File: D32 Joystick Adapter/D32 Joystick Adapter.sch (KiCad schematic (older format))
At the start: 12 parts, among them J1 Dragon 32, J2 Joystick, U1 4066

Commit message: Layout done
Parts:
- added M1, M2, M3, M4: Mounting, mounting:M3_pin, symbol mounting:Mounting
- C1: footprint Capacitors_THT:C_Disc_D4.7mm_W2.5mm_P5.00mm -> Capacitor_THT:C_Disc_D4.7mm_W2.5mm_P5.00mm
- J1: footprint (none) -> D32_Wirepads:OUTPUT_ZIP
- R1, R2, R3, R4, R5, R6, R7, R8: footprint (none) -> Resistor_THT:R_Axial_DIN0207_L6.3mm_D2.5mm_P10.16mm_Horizontal
- U1: footprint (none) -> Package_DIP:DIP-14_W7.62mm_Socket_LongPads
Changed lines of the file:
@@
 encoding utf-8
 Sheet 1 1
-Title ""
+Title "Dragon 32 Digital Joystick Adapter"
 Date ""
-Rev ""
+Rev "A"
 Comp ""
 Comment1 ""
 Comment2 ""
 Comment3 ""
-Comment4 ""
+Comment4 "Allows the use of Atari-style joysticks on the Dragon 32 computer."
 $EndDescr
 $Comp
@@
 F 0 "C1" H 685 6921 50  0000 R CNN
 F 1 "100nF" H 685 6830 50  0000 R CNN
-F 2 "Capacitors_THT:C_Disc_D4.7mm_W2.5mm_P5.00mm" H 838 6725 50  0001 C CNN
+F 2 "Capacitor_THT:C_Disc_D4.7mm_W2.5mm_P5.00mm" H 838 6725 50  0001 C CNN
 F 3 "~" H 800 6875 50  0001 C CNN
 	1    800  6875
@@
 F 0 "U1" H 4925 4527 50  0000 C CNN
 F 1 "4066" H 4925 4436 50  0000 C CNN
-F 2 "" H 4925 4700 50  0001 C CNN
+F 2 "Package_DIP:DIP-14_W7.62mm_Socket_LongPads" H 4925 4700 50  0001 C CNN
 F 3 "http://www.ti.com/lit/ds/symlink/cd4066b.pdf" H 4925 4700 50  0001 C CNN
 	1    4925 4700
@@
 F 0 "U1" H 4925 5277 50  0000 C CNN
 F 1 "4066" H 4925 5186 50  0000 C CNN
-F 2 "" H 4925 5450 50  0001 C CNN
+F 2 "Package_DIP:DIP-14_W7.62mm_Socket_LongPads" H 4925 5450 50  0001 C CNN
 F 3 "http://www.ti.com/lit/ds/symlink/cd4066b.pdf" H 4925 5450 50  0001 C CNN
 	2    4925 5450
@@
 F 0 "U1" H 7150 5277 50  0000 C CNN
 F 1 "4066" H 7150 5186 50  0000 C CNN
-F 2 "" H 7150 5450 50  0001 C CNN
+F 2 "Package_DIP:DIP-14_W7.62mm_Socket_LongPads" H 7150 5450 50  0001 C CNN
 F 3 "http://www.ti.com/lit/ds/symlink/cd4066b.pdf" H 7150 5450 50  0001 C CNN
 	3    7150 5450
@@
 F 0 "U1" H 7150 4527 50  0000 C CNN
 F 1 "4066" H 7150 4436 50  0000 C CNN
-F 2 "" H 7150 4700 50  0001 C CNN
+F 2 "Package_DIP:DIP-14_W7.62mm_Socket_LongPads" H 7150 4700 50  0001 C CNN
 F 3 "http://www.ti.com/lit/ds/symlink/cd4066b.pdf" H 7150 4700 50  0001 C CNN
 	4    7150 4700
@@
 F 0 "U1" H 1630 6921 50  0000 L CNN
 F 1 "4066" H 1630 6830 50  0000 L CNN
-F 2 "" H 1400 6875 50  0001 C CNN
+F 2 "Package_DIP:DIP-14_W7.62mm_Socket_LongPads" H 1400 6875 50  0001 C CNN
 F 3 "http://www.ti.com/lit/ds/symlink/cd4066b.pdf" H 1400 6875 50  0001 C CNN
 	5    1400 6875
@@
 F 0 "J1" H 6675 1350 50  0000 C CNN
 F 1 "Dragon 32" H 6675 1425 50  0000 C CNN
-F 2 "" H 6675 1925 50  0001 C CNN
+F 2 "D32_Wirepads:OUTPUT_ZIP" H 6675 1925 50  0001 C CNN
 F 3 "http://www.mouser.com/ds/2/18/40_c091_abd_e-75918.pdf" H 6675 1925 50  0001 C CNN
 	1    6675 1925
@@
 F 0 "R2" H 4492 4104 50  0000 R CNN
 F 1 "100k" H 4492 4195 50  0000 R CNN
-F 2 "" H 4550 4150 50  0001 C CNN
+F 2 "Resistor_THT:R_Axial_DIN0207_L6.3mm_D2.5mm_P10.16mm_Horizontal" H 4550 4150 50  0001 C CNN
 F 3 "~" H 4550 4150 50  0001 C CNN
 	1    4550 4150
@@
 F 0 "R1" H 4117 4104 50  0000 R CNN
 F 1 "100k" H 4117 4195 50  0000 R CNN
-F 2 "" H 4175 4150 50  0001 C CNN
+F 2 "Resistor_THT:R_Axial_DIN0207_L6.3mm_D2.5mm_P10.16mm_Horizontal" H 4175 4150 50  0001 C CNN
 F 3 "~" H 4175 4150 50  0001 C CNN
 	1    4175 4150
@@
 F 0 "R3" H 4867 4104 50  0000 R CNN
 F 1 "100k" H 4867 4195 50  0000 R CNN
-F 2 "" H 4925 4150 50  0001 C CNN
+F 2 "Resistor_THT:R_Axial_DIN0207_L6.3mm_D2.5mm_P10.16mm_Horizontal" H 4925 4150 50  0001 C CNN
 F 3 "~" H 4925 4150 50  0001 C CNN
 	1    4925 4150
@@
 F 0 "R4" H 4492 5579 50  0000 R CNN
 F 1 "100k" H 4492 5670 50  0000 R CNN
-F 2 "" H 4550 5625 50  0001 C CNN
+F 2 "Resistor_THT:R_Axial_DIN0207_L6.3mm_D2.5mm_P10.16mm_Horizontal" H 4550 5625 50  0001 C CNN
 F 3 "~" H 4550 5625 50  0001 C CNN
 	1    4550 5625
@@
 F 0 "R6" H 6717 4104 50  0000 R CNN
 F 1 "100k" H 6717 4195 50  0000 R CNN
-F 2 "" H 6775 4150 50  0001 C CNN
+F 2 "Resistor_THT:R_Axial_DIN0207_L6.3mm_D2.5mm_P10.16mm_Horizontal" H 6775 4150 50  0001 C CNN
 F 3 "~" H 6775 4150 50  0001 C CNN
 	1    6775 4150
@@
 F 0 "R5" H 6342 4104 50  0000 R CNN
 F 1 "100k" H 6342 4195 50  0000 R CNN
-F 2 "" H 6400 4150 50  0001 C CNN
+F 2 "Resistor_THT:R_Axial_DIN0207_L6.3mm_D2.5mm_P10.16mm_Horizontal" H 6400 4150 50  0001 C CNN
 F 3 "~" H 6400 4150 50  0001 C CNN
 	1    6400 4150
@@
 F 0 "R7" H 7092 4104 50  0000 R CNN
 F 1 "100k" H 7092 4195 50  0000 R CNN
-F 2 "" H 7150 4150 50  0001 C CNN
+F 2 "Resistor_THT:R_Axial_DIN0207_L6.3mm_D2.5mm_P10.16mm_Horizontal" H 7150 4150 50  0001 C CNN
 F 3 "~" H 7150 4150 50  0001 C CNN
 	1    7150 4150
@@
 F 0 "R8" H 6717 5579 50  0000 R CNN
 F 1 "100k" H 6717 5670 50  0000 R CNN
-F 2 "" H 6775 5625 50  0001 C CNN
+F 2 "Resistor_THT:R_Axial_DIN0207_L6.3mm_D2.5mm_P10.16mm_Horizontal" H 6775 5625 50  0001 C CNN
 F 3 "~" H 6775 5625 50  0001 C CNN
 	1    6775 5625
@@
 Text Notes 6225 2550 0    60   ~ 0
 (back of plug view)
+$Comp
+L mounting:Mounting M4
+U 1 1 6008691F
+P 11150 550
+F 0 "M4" H 11150 650 50  0001 C CNN
+F 1 "Mounting" H 11150 475 50  0001 C CNN
+F 2 "mounting:M3_pin" H 11150 550 50  0001 C CNN
+F 3 "~" H 11150 550 50  0001 C CNN
+	1    11150 550
+	1    0    0    -1
+$EndComp
+$Comp
+L mounting:Mounting M3
+U 1 1 600878AD
+P 11025 550
+F 0 "M3" H 11025 650 50  0001 C CNN
+F 1 "Mounting" H 11025 475 50  0001 C CNN
+F 2 "mounting:M3_pin" H 11025 550 50  0001 C CNN
+F 3 "~" H 11025 550 50  0001 C CNN
+	1    11025 550
+	1    0    0    -1
+$EndComp
+$Comp
+L mounting:Mounting M2
+U 1 1 60087CC9
+P 10900 550
+F 0 "M2" H 10900 650 50  0001 C CNN
+F 1 "Mounting" H 10900 475 50  0001 C CNN
+F 2 "mounting:M3_pin" H 10900 550 50  0001 C CNN
+F 3 "~" H 10900 550 50  0001 C CNN
+	1    10900 550
+	1    0    0    -1
+$EndComp
+$Comp
+L mounting:Mounting M1
+U 1 1 60088123
+P 10775 550
+F 0 "M1" H 10775 650 50  0001 C CNN
+F 1 "Mounting" H 10775 475 50  0001 C CNN
+F 2 "mounting:M3_pin" H 10775 550 50  0001 C CNN
+F 3 "~" H 10775 550 50  0001 C CNN
+	1    10775 550
+	1    0    0    -1
+$EndComp
 $EndSCHEMATC

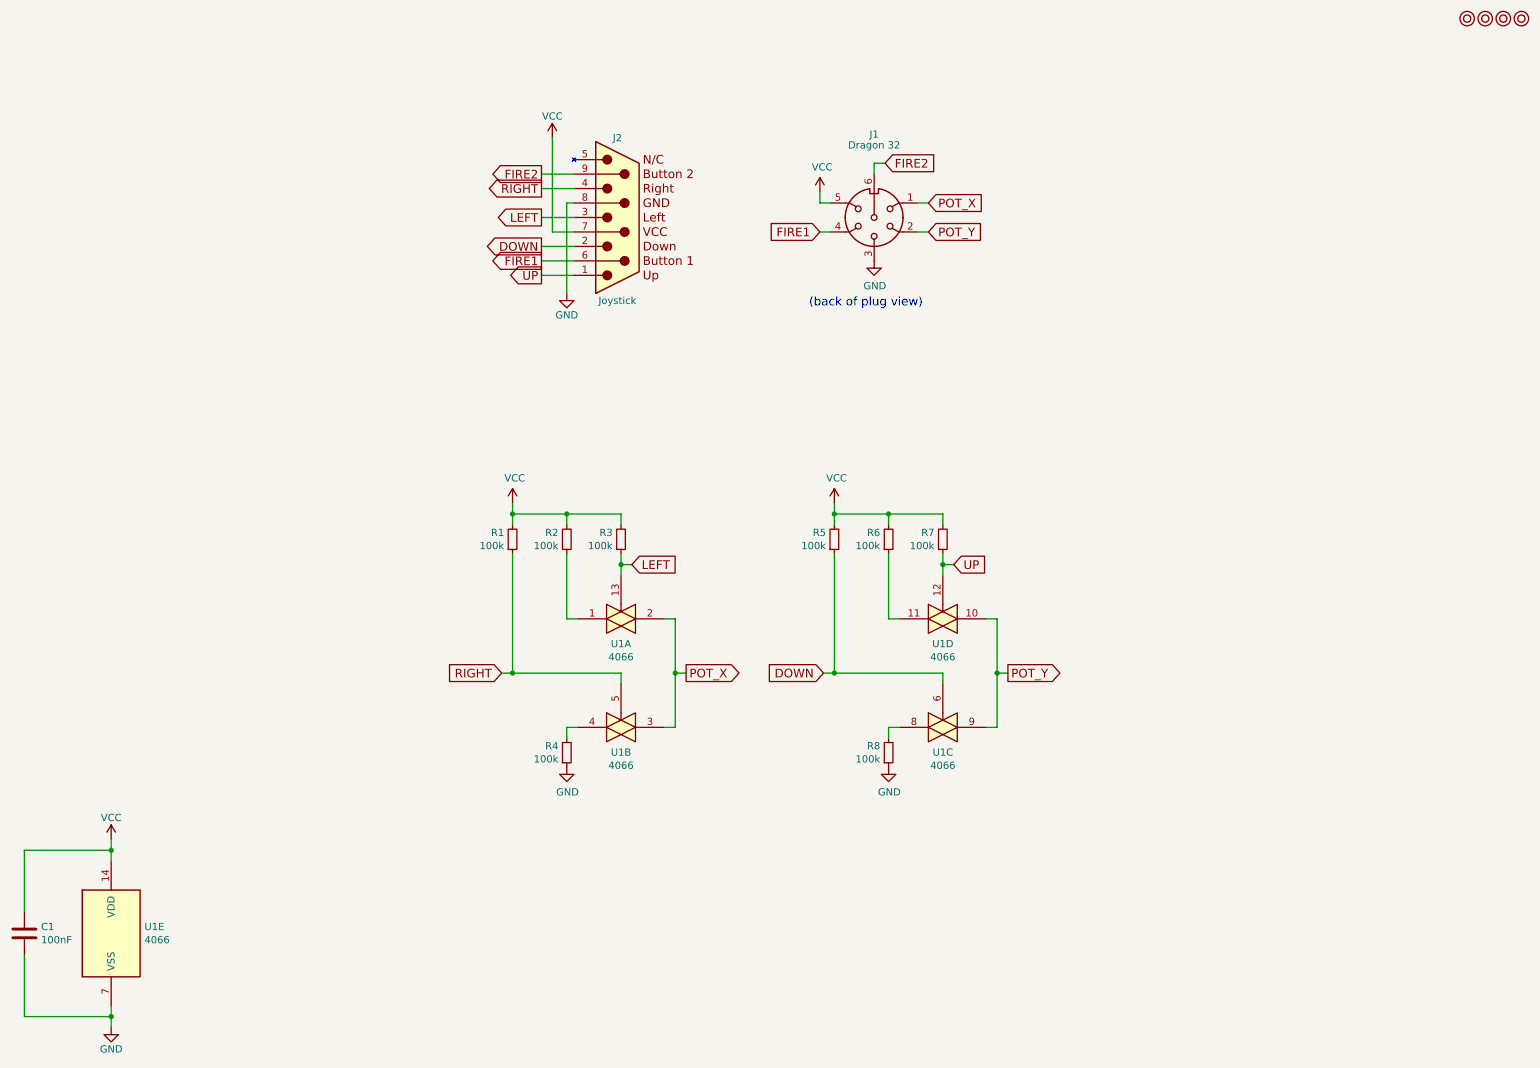
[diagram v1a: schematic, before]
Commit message: Added power jumper and changed resistor values
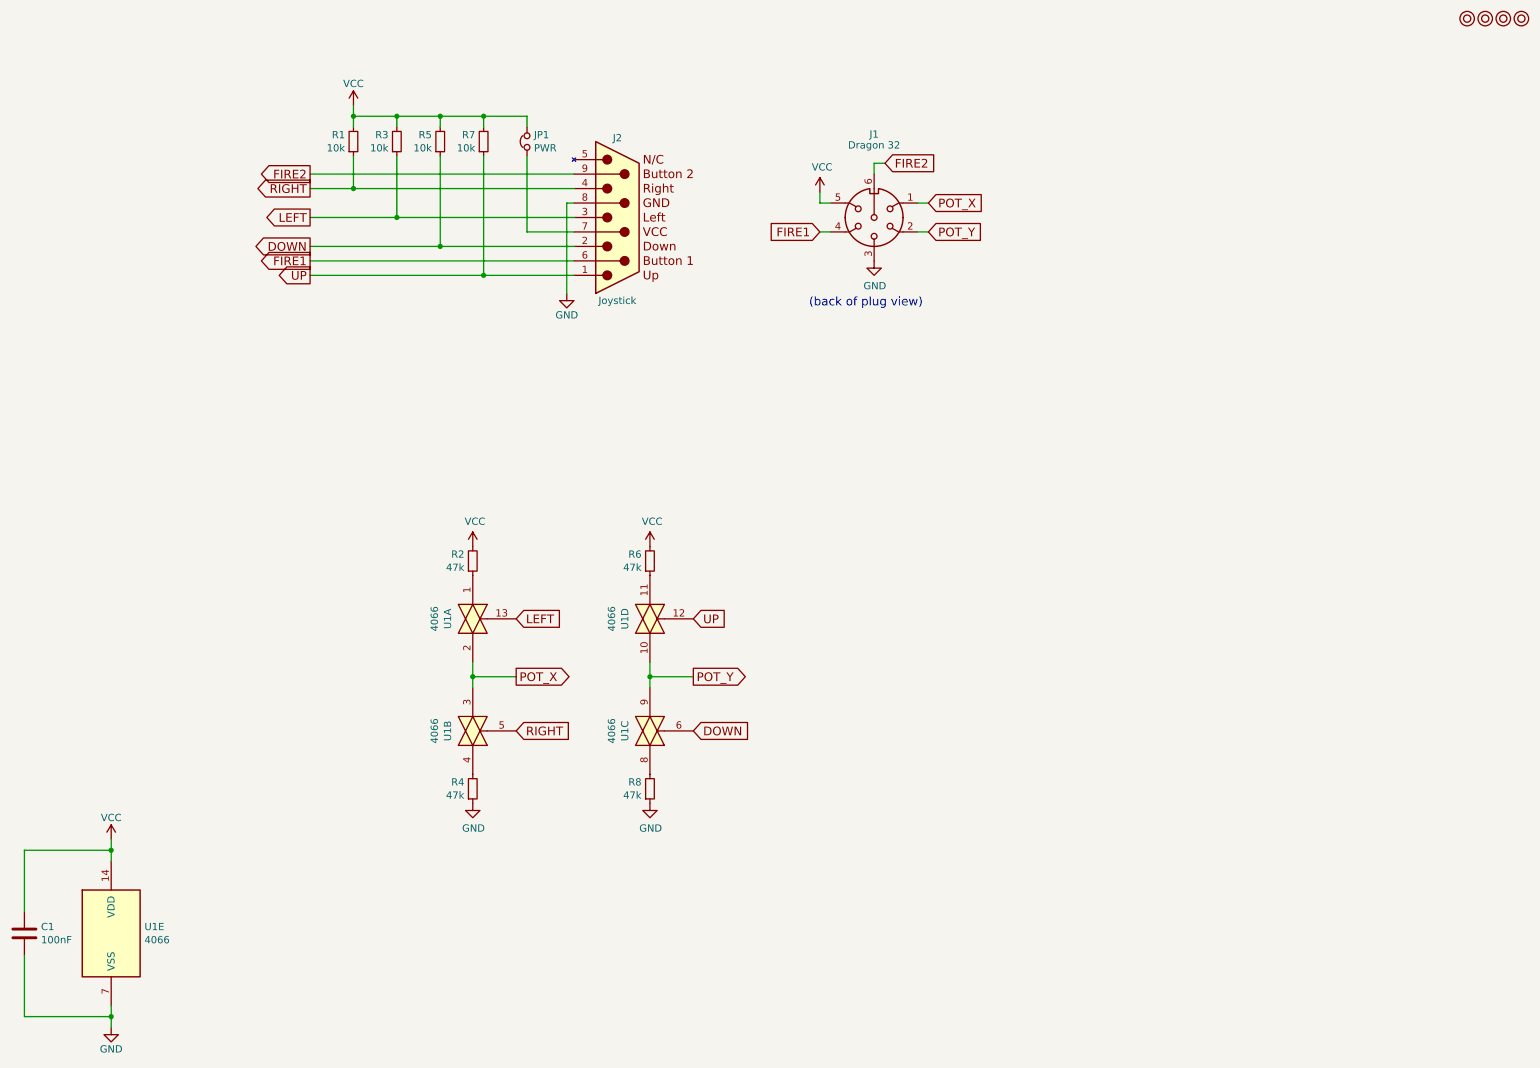
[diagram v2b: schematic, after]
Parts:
- added JP1: PWR, Connector_PinHeader_2.54mm:PinHeader_1x02_P2.54mm_Horizontal, symbol Device:Jumper_NC_Small
- R1, R3, R5, R7: value 100k -> 10k
- R2, R4, R6, R8: value 100k -> 47k
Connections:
- net VCC: now also JP1.2; no longer J2.7 (VCC)
- new net: J2.7 (VCC), JP1.1
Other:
- moved on the sheet: R1, R2, R3, R4, R5, R6, R7, R8, U1A, U1B, U1C, U1D
